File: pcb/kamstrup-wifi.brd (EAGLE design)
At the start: 36 x 42.5 mm, 6 parts

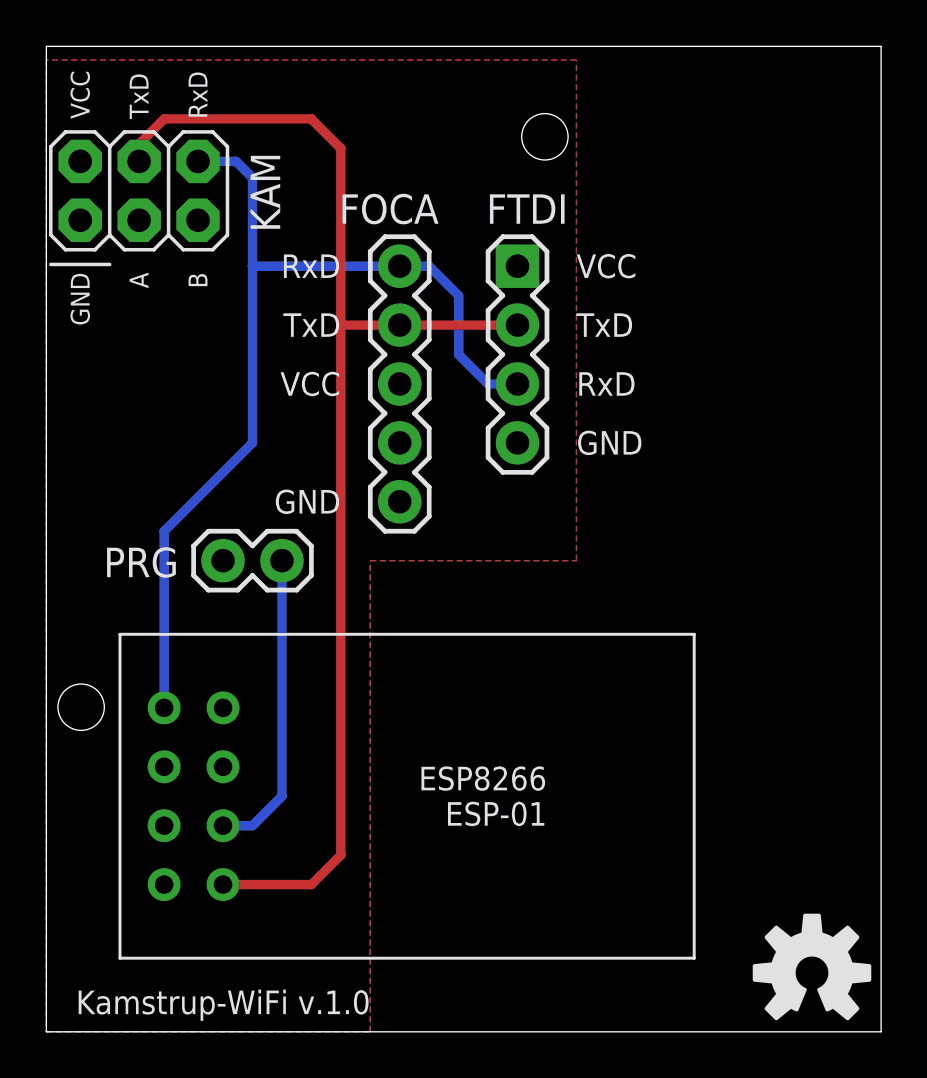
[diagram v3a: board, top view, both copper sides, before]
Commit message: pull down resistor on gpio0
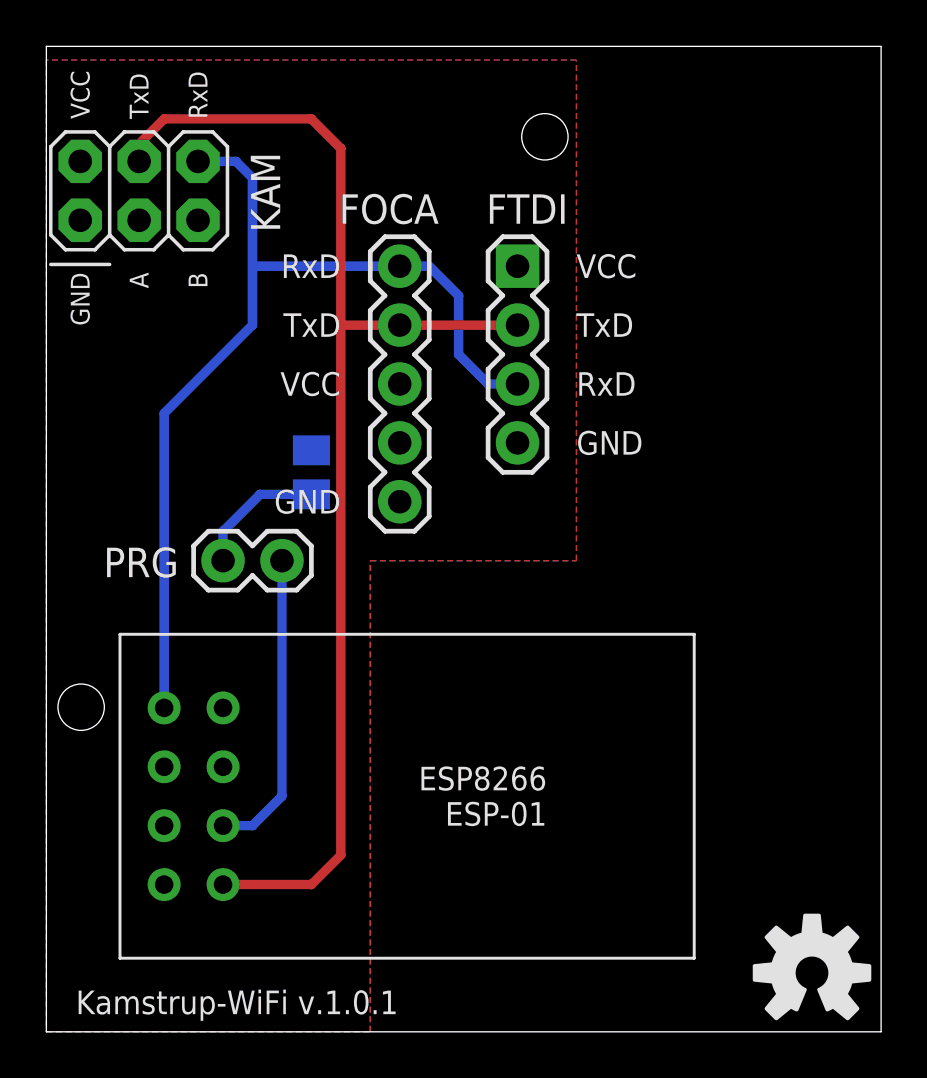
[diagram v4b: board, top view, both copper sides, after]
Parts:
- added R1: (no value), resistor:M0805
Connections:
- new net N$4: PRG.1, R1.2
- net GND: now also R1.1; no longer PRG.1
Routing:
- net N$4: track 0.00 -> 5.74 mm
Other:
- board text added: "Kamstrup-WiFi v.1.0.1"
- board text removed: "Kamstrup-WiFi v.1.0"
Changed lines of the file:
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@@
 <layers>
 <layer number="1" name="Top" color="4" fill="1" visible="yes" active="yes"/>
-<layer number="16" name="Bottom" color="1" fill="1" visible="yes" active="yes"/>
+<layer number="16" name="Bottom" color="1" fill="1" visible="no" active="yes"/>
 <layer number="17" name="Pads" color="2" fill="1" visible="yes" active="yes"/>
 <layer number="18" name="Vias" color="2" fill="1" visible="yes" active="yes"/>
@@
 <layer number="20" name="Dimension" color="15" fill="1" visible="yes" active="yes"/>
 <layer number="21" name="tPlace" color="7" fill="1" visible="yes" active="yes"/>
-<layer number="22" name="bPlace" color="7" fill="1" visible="yes" active="yes"/>
+<layer number="22" name="bPlace" color="7" fill="1" visible="no" active="yes"/>
 <layer number="23" name="tOrigins" color="15" fill="1" visible="yes" active="yes"/>
-<layer number="24" name="bOrigins" color="15" fill="1" visible="yes" active="yes"/>
+<layer number="24" name="bOrigins" color="15" fill="1" visible="no" active="yes"/>
 <layer number="25" name="tNames" color="7" fill="1" visible="yes" active="yes"/>
-<layer number="26" name="bNames" color="7" fill="1" visible="yes" active="yes"/>
+<layer number="26" name="bNames" color="7" fill="1" visible="no" active="yes"/>
 <layer number="27" name="tValues" color="7" fill="1" visible="yes" active="yes"/>
-<layer number="28" name="bValues" color="7" fill="1" visible="yes" active="yes"/>
+<layer number="28" name="bValues" color="7" fill="1" visible="no" active="yes"/>
 <layer number="29" name="tStop" color="7" fill="3" visible="yes" active="yes"/>
-<layer number="30" name="bStop" color="7" fill="6" visible="yes" active="yes"/>
+<layer number="30" name="bStop" color="7" fill="6" visible="no" active="yes"/>
 <layer number="31" name="tCream" color="7" fill="4" visible="yes" active="yes"/>
-<layer number="32" name="bCream" color="7" fill="5" visible="yes" active="yes"/>
+<layer number="32" name="bCream" color="7" fill="5" visible="no" active="yes"/>
 <layer number="33" name="tFinish" color="6" fill="3" visible="yes" active="yes"/>
-<layer number="34" name="bFinish" color="6" fill="6" visible="yes" active="yes"/>
+<layer number="34" name="bFinish" color="6" fill="6" visible="no" active="yes"/>
 <layer number="35" name="tGlue" color="7" fill="4" visible="yes" active="yes"/>
-<layer number="36" name="bGlue" color="7" fill="5" visible="yes" active="yes"/>
+<layer number="36" name="bGlue" color="7" fill="5" visible="no" active="yes"/>
 <layer number="37" name="tTest" color="7" fill="1" visible="yes" active="yes"/>
-<layer number="38" name="bTest" color="7" fill="1" visible="yes" active="yes"/>
+<layer number="38" name="bTest" color="7" fill="1" visible="no" active="yes"/>
 <layer number="39" name="tKeepout" color="4" fill="11" visible="yes" active="yes"/>
-<layer number="40" name="bKeepout" color="1" fill="11" visible="yes" active="yes"/>
+<layer number="40" name="bKeepout" color="1" fill="11" visible="no" active="yes"/>
 <layer number="41" name="tRestrict" color="4" fill="10" visible="yes" active="yes"/>
-<layer number="42" name="bRestrict" color="1" fill="10" visible="yes" active="yes"/>
+<layer number="42" name="bRestrict" color="1" fill="10" visible="no" active="yes"/>
 <layer number="43" name="vRestrict" color="2" fill="10" visible="yes" active="yes"/>
 <layer number="44" name="Drills" color="7" fill="1" visible="yes" active="yes"/>
@@
 <layer number="50" name="dxf" color="7" fill="1" visible="no" active="no"/>
 <layer number="51" name="tDocu" color="7" fill="1" visible="yes" active="yes"/>
-<layer number="52" name="bDocu" color="7" fill="1" visible="yes" active="yes"/>
+<layer number="52" name="bDocu" color="7" fill="1" visible="no" active="yes"/>
 <layer number="53" name="tGND_GNDA" color="7" fill="9" visible="no" active="no"/>
 <layer number="54" name="bGND_GNDA" color="1" fill="9" visible="no" active="no"/>
@@
 <layer number="97" name="Info" color="7" fill="1" visible="no" active="no"/>
 <layer number="98" name="Guide" color="6" fill="1" visible="no" active="no"/>
+<layer number="99" name="SpiceOrder" color="5" fill="1" visible="no" active="no"/>
 <layer number="100" name="Muster" color="7" fill="1" visible="no" active="no"/>
 <layer number="101" name="Patch_Top" color="12" fill="4" visible="yes" active="yes"/>
@@
 <layer number="104" name="Name" color="16" fill="1" visible="yes" active="yes"/>
 <layer number="105" name="tPlate" color="7" fill="1" visible="yes" active="yes"/>
-<layer number="106" name="bPlate" color="7" fill="1" visible="yes" active="yes"/>
+<layer number="106" name="bPlate" color="7" fill="1" visible="no" active="yes"/>
 <layer number="107" name="Crop" color="7" fill="1" visible="yes" active="yes"/>
 <layer number="108" name="tplace-old" color="10" fill="1" visible="no" active="yes"/>
@@
 <layer number="116" name="Patch_BOT" color="9" fill="4" visible="yes" active="yes"/>
 <layer number="121" name="_tsilk" color="7" fill="1" visible="yes" active="yes"/>
-<layer number="122" name="_bsilk" color="7" fill="1" visible="yes" active="yes"/>
+<layer number="122" name="_bsilk" color="7" fill="1" visible="no" active="yes"/>
 <layer number="125" name="_tNames" color="7" fill="1" visible="yes" active="yes"/>
 <layer number="144" name="Drill_legend" color="7" fill="1" visible="yes" active="yes"/>
@@
 <text x="21.59" y="10.16" size="1.016" layer="25" align="center-right">ESP8266
 ESP-01</text>
-<text x="1.27" y="1.27" size="1.016" layer="25" rot="R180" align="center-right">Kamstrup-WiFi v.1.0</text>
+<text x="1.27" y="1.27" size="1.016" layer="25" rot="R180" align="center-right">Kamstrup-WiFi v.1.0.1</text>
 </plain>
 <attributes>
@@
 </element>
 <element name="U$2" library="SparkFun-Aesthetics" package="OSHW-LOGO-M" value="" x="33.02" y="2.54"/>
+<element name="R1" library="resistor" package="M0805" value="" x="11.43" y="24.13" rot="MR270">
+<attribute name="SPICEPREFIX" value="R" x="11.43" y="24.13" size="1.016" layer="28" rot="MR270" display="off"/>
+</element>
 </elements>
 <signals>
@@
 <contactref element="FTDI" pad="4"/>
 <contactref element="FOCA" pad="5"/>
-<polygon width="0.4064" layer="16" isolate="0.6096">
+<polygon width="0.4064" layer="16" isolate="0.4064">
 <vertex x="0" y="0"/>
 <vertex x="13.97" y="0"/>
@@
 <vertex x="0" y="41.91"/>
 </polygon>
-<contactref element="PRG" pad="1"/>
+<contactref element="R1" pad="1"/>
 </signal>
 <signal name="3.3V">
@@
 <contactref element="FTDI" pad="1"/>
 <contactref element="FOCA" pad="3"/>
-<polygon width="0.4064" layer="1" isolate="0.6096">
+<polygon width="0.4064" layer="1" isolate="0.4064">
 <vertex x="0" y="0"/>
 <vertex x="13.97" y="0"/>
@@
 <wire x1="8.18" y1="37.54" x2="8.89" y2="36.83" width="0.4064" layer="16"/>
 <wire x1="8.89" y1="36.83" x2="8.89" y2="33.02" width="0.4064" layer="16"/>
-<wire x1="8.89" y1="33.02" x2="8.89" y2="25.4" width="0.4064" layer="16"/>
-<wire x1="8.89" y1="25.4" x2="5.08" y2="21.59" width="0.4064" layer="16"/>
-<wire x1="5.08" y1="21.59" x2="5.08" y2="13.97" width="0.4064" layer="16"/>
+<wire x1="8.89" y1="33.02" x2="8.89" y2="30.48" width="0.4064" layer="16"/>
+<wire x1="8.89" y1="30.48" x2="5.08" y2="26.67" width="0.4064" layer="16"/>
+<wire x1="5.08" y1="26.67" x2="5.08" y2="13.97" width="0.4064" layer="16"/>
 <wire x1="15.24" y1="33.02" x2="8.89" y2="33.02" width="0.4064" layer="16"/>
 </signal>
@@
 <wire x1="10.16" y1="10.16" x2="10.16" y2="20.32" width="0.4064" layer="16"/>
 </signal>
+<signal name="N$4">
+<contactref element="PRG" pad="1"/>
+<contactref element="R1" pad="2"/>
+<wire x1="11.43" y1="23.18" x2="9.21" y2="23.18" width="0.4064" layer="16"/>
+<wire x1="9.21" y1="23.18" x2="7.62" y2="21.59" width="0.4064" layer="16"/>
+<wire x1="7.62" y1="21.59" x2="7.62" y2="20.32" width="0.4064" layer="16"/>
+</signal>
 </signals>

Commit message: pull down resisistor value = 10k
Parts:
- R1: value (none) -> 10k
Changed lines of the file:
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@@
 </element>
 <element name="U$2" library="SparkFun-Aesthetics" package="OSHW-LOGO-M" value="" x="33.02" y="2.54"/>
-<element name="R1" library="resistor" package="M0805" value="" x="11.43" y="24.13" rot="MR270">
+<element name="R1" library="resistor" package="M0805" value="10k" x="11.43" y="24.13" rot="MR270">
 <attribute name="SPICEPREFIX" value="R" x="11.43" y="24.13" size="1.016" layer="28" rot="MR270" display="off"/>
 </element>
